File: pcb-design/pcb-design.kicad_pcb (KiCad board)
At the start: 2 copper layers, 43 parts, among them M1 CSD19502Q5B, Q1 BC846, U1 UCC2813D-1

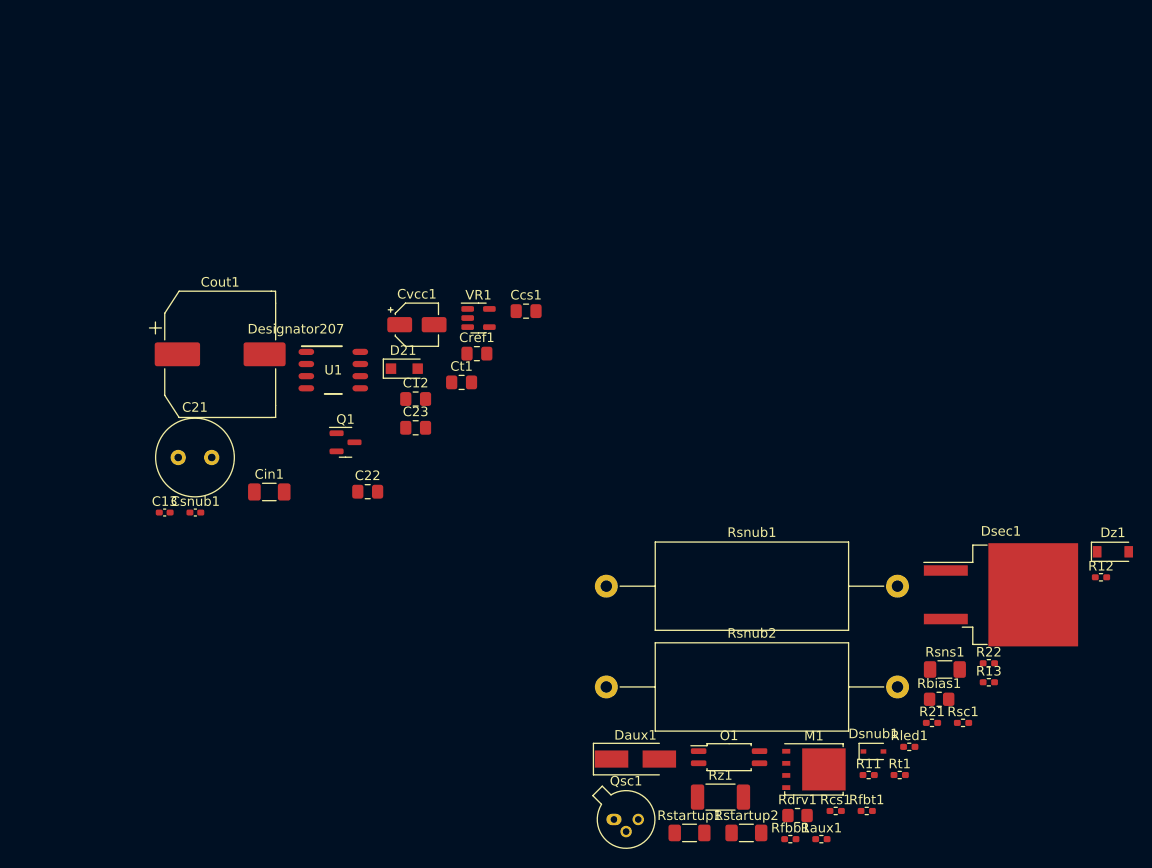
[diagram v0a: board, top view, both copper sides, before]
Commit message: Transformer footprint is added.
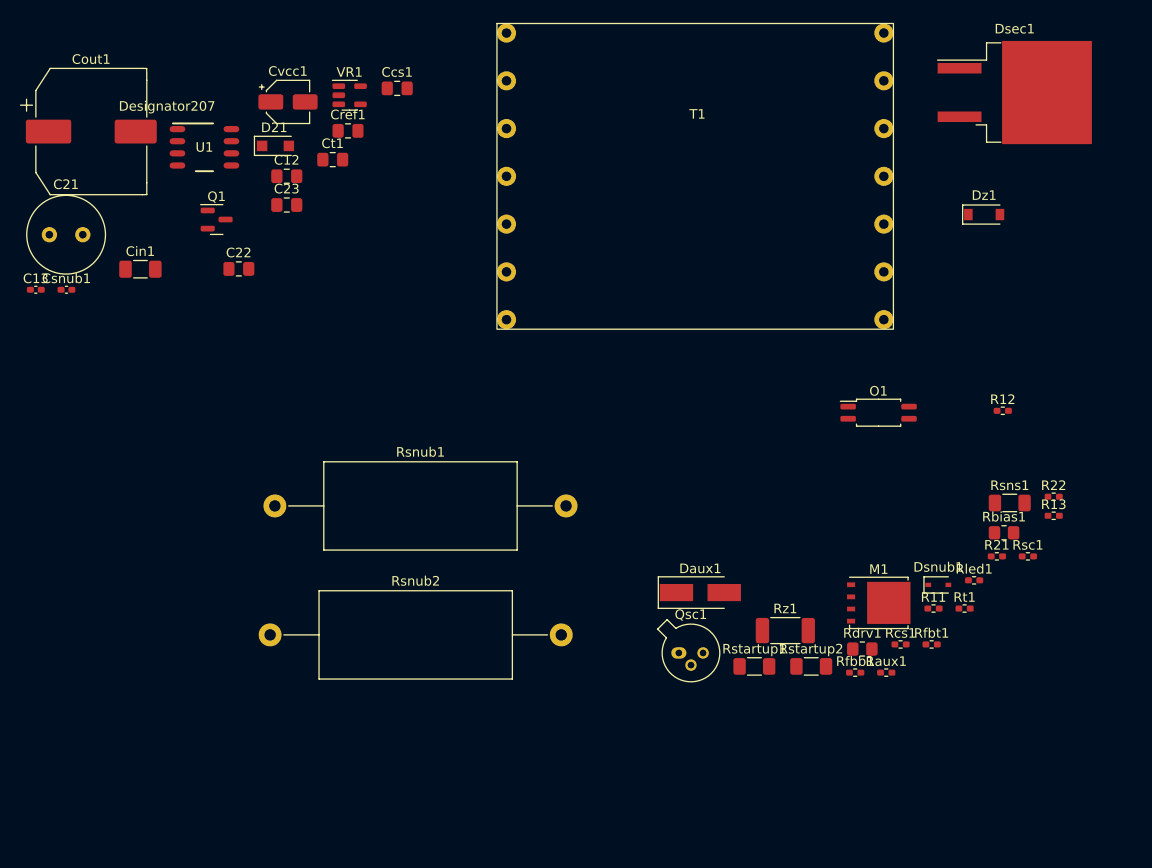
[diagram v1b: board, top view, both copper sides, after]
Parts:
- added T1: Transformer_1P_2S, CUSTOM_FOOTPRINTS:Custom_Transformer-P0.5-7, F.Cu at (135.0, 62.0)
- moved Dsec1 52.6 mm to (168.2, 53.2)
- moved O1 39.3 mm to (153.9, 86.7)
- moved Dz1 37.8 mm to (165.0, 66.0)
- moved Rsnub1 35.7 mm to (90.8, 96.5)
- moved Rsnub2 35.6 mm to (90.3, 110.0)
- moved Q1 26.9 mm to (84.7, 66.5)
- moved C21 26.9 mm to (67.2, 68.1)
- moved C22 26.9 mm to (87.0, 71.7)
- moved Cin1 26.9 mm to (76.7, 71.7)
- moved Cref1 26.9 mm to (98.4, 57.2)
- moved Cvcc1 26.9 mm to (92.1, 54.2)
- moved C12 26.9 mm to (92.0, 62.0)
- moved Ccs1 26.9 mm to (103.6, 52.8)
- moved Cout1 26.9 mm to (71.5, 57.3)
- moved Csnub1 26.9 mm to (68.9, 73.9)
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
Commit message: Schematic is corrected. PCB Design is added.
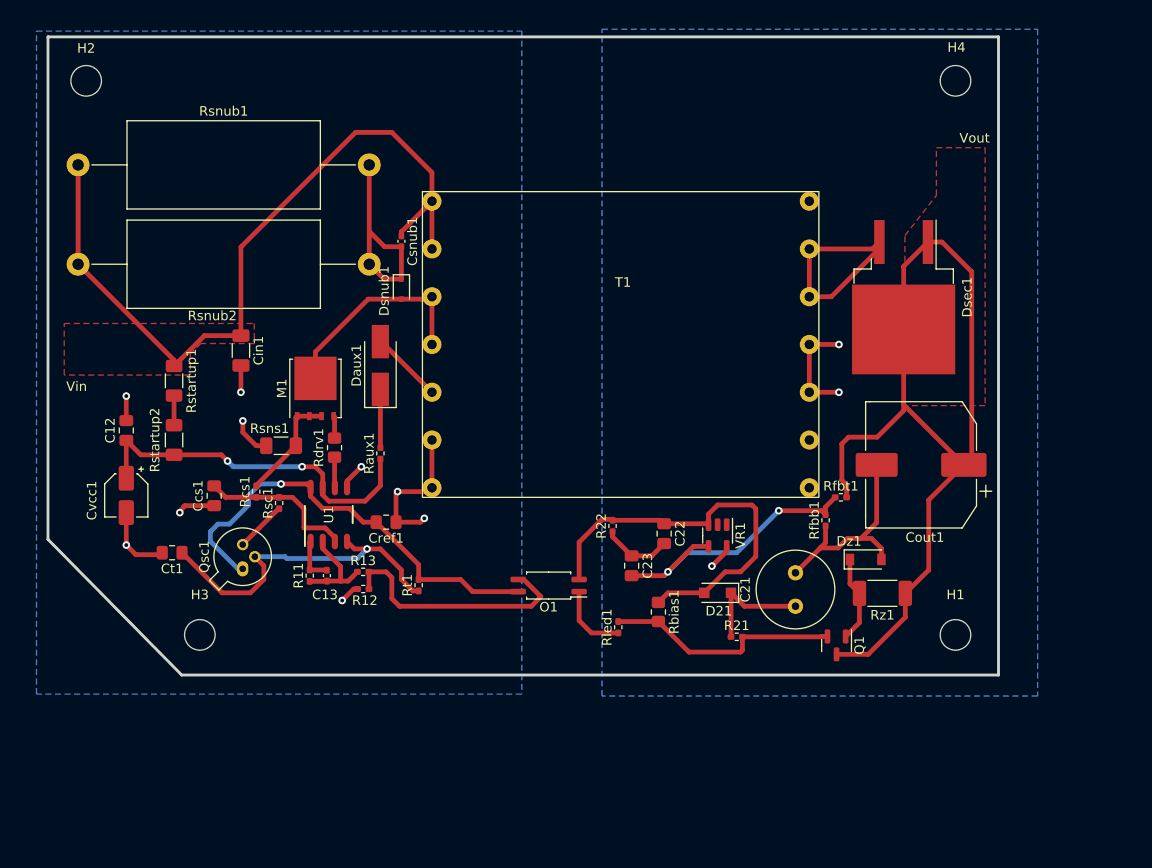
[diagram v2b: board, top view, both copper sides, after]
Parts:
- added H1: MountingHole, MountingHole:MountingHole_3.2mm_M3, F.Cu at (162.0, 110.0)
- added H2: MountingHole, MountingHole:MountingHole_3.2mm_M3, F.Cu at (71.0, 52.0)
- added H3: MountingHole, MountingHole:MountingHole_3.2mm_M3, F.Cu at (82.9, 110.0)
- added H4: MountingHole, MountingHole:MountingHole_3.2mm_M3, F.Cu at (162.0, 52.0)
- moved Cout1 93.6 mm to (158.4, 92.2), turned to 180 degrees
- moved C21 87.2 mm to (145.2, 107.0), turned to 90 degrees
- moved Q1 78.7 mm to (149.6, 111.1), turned to -90 degrees
- moved Rsc1 78.6 mm to (91.2, 96.2), turned to 90 degrees
- moved Rsns1 76.5 mm to (91.4, 90.2)
- moved R13 72.5 mm to (100.0, 103.4)
- moved Rstartup2 70.8 mm to (80.2, 89.6), turned to -90 degrees
- moved R12 69.5 mm to (100.0, 105.2)
- moved Rcs1 69.3 mm to (88.8, 95.0), turned to 90 degrees
- moved Rstartup1 67.7 mm to (80.2, 83.4), turned to -90 degrees
- moved D21 65.8 mm to (137.1, 105.6), turned to 180 degrees
- moved R11 65.4 mm to (94.4, 103.8), turned to 90 degrees
- moved Dsnub1 64.2 mm to (104.0, 73.8), turned to -90 degrees
- moved M1 63.1 mm to (95.0, 84.2), turned to 90 degrees
- moved VR1 60.1 mm to (137.1, 99.6), turned to -90 degrees
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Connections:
- M1 pad 5: Net-(Daux1-Pad1) -> Net-(Dsnub1-Pad2)
- Rt1 pad 1: Net-(Cref1-Pad2) -> Net-(Ct1-Pad1)
- T1 pad 1: GND -> VDC
- T1 pad 10: (no net) -> Net-(Dsec1-Pad2)
- T1 pad 11: (no net) -> GND
- T1 pad 12: (no net) -> GND
- T1 pad 2: Net-(Dsec1-Pad2) -> VDC
- T1 pad 3: Net-(Daux1-Pad2) -> Net-(Dsnub1-Pad2)
- T1 pad 4: GNDREF -> Net-(Dsnub1-Pad2)
- T1 pad 5: Net-(Dsnub1-Pad2) -> Net-(Daux1-Pad2)
- T1 pad 6: VDC -> GNDREF
- T1 pad 7: (no net) -> GNDREF
- T1 pad 9: (no net) -> Net-(Dsec1-Pad2)
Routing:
- net Vout: track 0.00 -> 95.1 mm
- net VDC: track 0.00 -> 82.5 mm
- net Net-(Cref1-Pad2): track 0.00 -> 46.6 mm, vias 0 -> 1
- net Net-(C22-Pad1): track 0.00 -> 42.5 mm
- net GNDREF: track 0.00 -> 41.3 mm, vias 0 -> 9
- net Net-(C12-Pad1): track 0.00 -> 38.0 mm, vias 0 -> 2
- net GND: track 0.00 -> 36.9 mm, vias 0 -> 3
- net Net-(Ct1-Pad1): track 0.00 -> 36.1 mm, vias 0 -> 1
- net Net-(C23-Pad2): track 0.00 -> 30.9 mm, vias 0 -> 2
- net Net-(O1-Pad3): track 0.00 -> 26.1 mm
- net Net-(Q1-Pad2): track 0.00 -> 24.7 mm
- net Net-(Dsec1-Pad2): track 0.00 -> 22.7 mm
- net Net-(Dsnub1-Pad2): track 0.00 -> 22.4 mm
- net Net-(Csnub1-Pad2): track 0.00 -> 21.8 mm
- net Net-(Ccs1-Pad2): track 0.00 -> 16.5 mm
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- added copper zone on B.Cu, net GND
- added copper zone on B.Cu, net GNDREF
- added copper zone on F.Cu, net VDC
- added copper zone on F.Cu, net Vout
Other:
- board outline added: 99.5 x 66.8 mm
- board text added: "P_GND"
- board text added: "S_GND"
- board text added: "Vin"
- board text added: "Vout"

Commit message: Case design is added and some minor fixes on PCB design.
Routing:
- net Vout: track 95.1 -> 58.4 mm
- net Net-(Dsec1-Pad2): track 22.7 -> 0.69 mm
- net VDC: track 82.5 -> 65.8 mm
- net GND: track 36.9 -> 25.7 mm, vias 3 -> 1
- net GNDREF: track 41.3 -> 32.2 mm, vias 9 -> 7
- net Net-(M1-Pad1): track 11.6 -> 5.92 mm
- net Net-(Csnub1-Pad2): track 21.8 -> 17.7 mm
- net Net-(O1-Pad3): track 26.1 -> 26.9 mm
- added copper zone on F.Cu, net Net-(Dsec1-Pad2)
- added copper zone on F.Cu, net Net-(M1-Pad1)
